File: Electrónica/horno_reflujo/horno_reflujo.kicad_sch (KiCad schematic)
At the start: 42 parts, among them J1 LevelShifter, J10 ssr1, J11 ssr2, J12 encoder, J13 Max6675_modulo2, J14 Max6675_modulo3, J15 Max6675_modulo4, J2 LevelShifter, J3 Display Oled I2C, J4 Max6675_modulo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

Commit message: Update pcb
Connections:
- net +3.3V: now also J1.3 (Pin_3); no longer J1.4 (Pin_4)
- net +5V: now also J2.4 (Pin_4), J3.2 (Pin_2); no longer J2.3 (Pin_3), J3.1 (Pin_1)
- net GND: now also J1.4 (Pin_4), J2.3 (Pin_3), J3.1 (Pin_1); no longer J1.3 (Pin_3), J2.4 (Pin_4), J3.4 (Pin_4)
- net at J2.1 (Pin_1): now also J3.3 (Pin_3); no longer J3.2 (Pin_2)
- net at J2.2 (Pin_2): now also J3.4 (Pin_4); no longer J3.3 (Pin_3)
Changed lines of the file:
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@@
 	(wire
 		(pts
+			(xy 180.34 130.81) (xy 185.42 130.81)
+		)
+		(stroke
+			(width 0)
+			(type default)
+		)
+	)
+	(wire
+		(pts
 			(xy 171.45 87.63) (xy 172.72 87.63)
 		)
@@
 	(wire
 		(pts
+			(xy 157.48 135.89) (xy 185.42 135.89)
+		)
+		(stroke
+			(width 0)
+			(type default)
+		)
+	)
+	(wire
+		(pts
 			(xy 194.31 90.17) (xy 195.58 90.17)
 		)
@@
 	(wire
 		(pts
+			(xy 157.48 119.38) (xy 157.48 135.89)
+		)
+		(stroke
+			(width 0)
+			(type default)
+		)
+	)
+	(wire
+		(pts
 			(xy 35.56 166.37) (xy 43.18 166.37)
 		)
@@
 	(wire
 		(pts
-			(xy 147.32 77.47) (xy 147.32 78.74)
+			(xy 153.67 121.92) (xy 153.67 138.43)
 		)
 		(stroke
@@
 	(wire
 		(pts
-			(xy 172.72 161.29) (xy 172.72 166.37)
+			(xy 147.32 77.47) (xy 147.32 78.74)
 		)
 		(stroke
@@
 	(wire
 		(pts
-			(xy 27.94 80.01) (xy 26.67 80.01)
+			(xy 172.72 161.29) (xy 172.72 166.37)
 		)
 		(stroke
@@
 	(wire
 		(pts
-			(xy 68.58 135.89) (xy 71.12 135.89)
+			(xy 27.94 80.01) (xy 26.67 80.01)
 		)
 		(stroke
@@
 	(wire
 		(pts
-			(xy 237.49 66.04) (xy 240.03 66.04)
+			(xy 68.58 135.89) (xy 71.12 135.89)
 		)
 		(stroke
@@
 	(wire
 		(pts
-			(xy 57.15 33.02) (xy 57.15 38.1)
+			(xy 237.49 66.04) (xy 240.03 66.04)
 		)
 		(stroke
@@
 	(wire
 		(pts
-			(xy 153.67 135.89) (xy 185.42 135.89)
+			(xy 57.15 33.02) (xy 57.15 38.1)
 		)
 		(stroke
@@
 	(wire
 		(pts
-			(xy 157.48 133.35) (xy 157.48 119.38)
+			(xy 68.58 176.53) (xy 73.66 176.53)
 		)
 		(stroke
@@
 	(wire
 		(pts
-			(xy 68.58 176.53) (xy 73.66 176.53)
+			(xy 44.45 78.74) (xy 44.45 80.01)
 		)
 		(stroke
@@
 	(wire
 		(pts
-			(xy 44.45 78.74) (xy 44.45 80.01)
+			(xy 128.27 66.04) (xy 127 66.04)
 		)
 		(stroke
@@
 	(wire
 		(pts
-			(xy 128.27 66.04) (xy 127 66.04)
+			(xy 35.56 87.63) (xy 35.56 90.17)
 		)
 		(stroke
@@
 	(wire
 		(pts
-			(xy 35.56 87.63) (xy 35.56 90.17)
+			(xy 153.67 138.43) (xy 185.42 138.43)
 		)
 		(stroke
@@
 	(wire
 		(pts
-			(xy 180.34 130.81) (xy 185.42 130.81)
+			(xy 179.07 133.35) (xy 185.42 133.35)
 		)
 		(stroke
@@
 	(wire
 		(pts
-			(xy 157.48 133.35) (xy 185.42 133.35)
-		)
-		(stroke
-			(width 0)
-			(type default)
-		)
-	)
-	(wire
-		(pts
 			(xy 166.37 95.25) (xy 172.72 95.25)
 		)
@@
 	(wire
 		(pts
-			(xy 179.07 138.43) (xy 185.42 138.43)
-		)
-		(stroke
-			(width 0)
-			(type default)
-		)
-	)
-	(wire
-		(pts
 			(xy 130.81 167.64) (xy 132.08 167.64)
 		)
@@
 	(wire
 		(pts
-			(xy 153.67 135.89) (xy 153.67 121.92)
-		)
-		(stroke
-			(width 0)
-			(type default)
-		)
-	)
-	(wire
-		(pts
 			(xy 194.31 57.15) (xy 194.31 49.53)
 		)
@@
 	(symbol
 		(lib_id "power:GND")
-		(at 144.78 127 90)
+		(at 144.78 124.46 90)
 		(unit 1)
 		(exclude_from_sim no)
@@
 		(on_board yes)
 		(dnp no)
-		(fields_autoplaced yes)
 		(property "Reference" "#PWR024"
-			(at 151.13 127 0)
+			(at 151.13 124.46 0)
 			(effects
 				(font
@@
 		)
 		(property "Value" "GND"
-			(at 148.59 126.9999 90)
+			(at 147.828 124.46 90)
 			(effects
 				(font
@@
 		)
 		(property "Footprint" ""
-			(at 144.78 127 0)
+			(at 144.78 124.46 0)
 			(effects
 				(font
@@
 		)
 		(property "Datasheet" ""
-			(at 144.78 127 0)
+			(at 144.78 124.46 0)
 			(effects
 				(font
@@
 		)
 		(property "Description" "Power symbol creates a global label with name \"GND\" , ground"
-			(at 144.78 127 0)
+			(at 144.78 124.46 0)
 			(effects
 				(font
@@
 	(symbol
 		(lib_id "power:+5V")
-		(at 180.34 130.81 90)
+		(at 179.07 133.35 90)
 		(mirror x)
 		(unit 1)
@@
 		(fields_autoplaced yes)
 		(property "Reference" "#PWR023"
-			(at 184.15 130.81 0)
+			(at 182.88 133.35 0)
 			(effects
 				(font
@@
 		)
 		(property "Value" "+5V"
-			(at 176.53 130.8099 90)
+			(at 175.26 133.3499 90)
 			(effects
 				(font
@@
 		)
 		(property "Footprint" ""
-			(at 180.34 130.81 0)
+			(at 179.07 133.35 0)
 			(effects
 				(font
@@
 		)
 		(property "Datasheet" ""
-			(at 180.34 130.81 0)
+			(at 179.07 133.35 0)
 			(effects
 				(font
@@
 		)
 		(property "Description" "Power symbol creates a global label with name \"+5V\""
-			(at 180.34 130.81 0)
+			(at 179.07 133.35 0)
 			(effects
 				(font
@@
 	(symbol
 		(lib_id "PCM_4ms_Power-symbol:+3.3V")
-		(at 123.19 124.46 90)
+		(at 123.19 127 90)
 		(unit 1)
 		(exclude_from_sim no)
@@
 		(on_board yes)
 		(dnp no)
-		(fields_autoplaced yes)
 		(property "Reference" "#PWR051"
-			(at 127 124.46 0)
+			(at 127 127 0)
 			(effects
 				(font
@@
 		)
 		(property "Value" "+3.3V"
-			(at 119.38 124.4599 90)
+			(at 119.38 127 90)
 			(effects
 				(font
@@
 		)
 		(property "Footprint" ""
-			(at 123.19 124.46 0)
+			(at 123.19 127 0)
 			(effects
 				(font
@@
 		)
 		(property "Datasheet" ""
-			(at 123.19 124.46 0)
+			(at 123.19 127 0)
 			(effects
 				(font
@@
 		)
 		(property "Description" ""
-			(at 123.19 124.46 0)
+			(at 123.19 127 0)
 			(effects
 				(font
@@
 	(symbol
 		(lib_id "power:GND")
-		(at 123.19 127 270)
+		(at 123.19 124.46 270)
 		(unit 1)
 		(exclude_from_sim no)
@@
 		(fields_autoplaced yes)
 		(property "Reference" "#PWR020"
-			(at 116.84 127 0)
+			(at 116.84 124.46 0)
 			(effects
 				(font
@@
 		)
 		(property "Value" "GND"
-			(at 119.38 126.9999 90)
+			(at 119.38 124.4599 90)
 			(effects
 				(font
@@
 		)
 		(property "Footprint" ""
-			(at 123.19 127 0)
+			(at 123.19 124.46 0)
 			(effects
 				(font
@@
 		)
 		(property "Datasheet" ""
-			(at 123.19 127 0)
+			(at 123.19 124.46 0)
 			(effects
 				(font
@@
 		)
 		(property "Description" "Power symbol creates a global label with name \"GND\" , ground"
-			(at 123.19 127 0)
+			(at 123.19 124.46 0)
 			(effects
 				(font
@@
 	(symbol
 		(lib_id "power:GND")
-		(at 179.07 138.43 270)
+		(at 180.34 130.81 270)
 		(mirror x)
 		(unit 1)
@@
 		(fields_autoplaced yes)
 		(property "Reference" "#PWR022"
-			(at 172.72 138.43 0)
+			(at 173.99 130.81 0)
 			(effects
 				(font
@@
 		)
 		(property "Value" "GND"
-			(at 175.26 138.4299 90)
+			(at 176.53 130.8099 90)
 			(effects
 				(font
@@
 		)
 		(property "Footprint" ""
-			(at 179.07 138.43 0)
+			(at 180.34 130.81 0)
 			(effects
 				(font
@@
 		)
 		(property "Datasheet" ""
-			(at 179.07 138.43 0)
+			(at 180.34 130.81 0)
 			(effects
 				(font
@@
 		)
 		(property "Description" "Power symbol creates a global label with name \"GND\" , ground"
-			(at 179.07 138.43 0)
+			(at 180.34 130.81 0)
 			(effects
 				(font
@@
 	(symbol
 		(lib_id "power:+5V")
-		(at 144.78 124.46 270)
+		(at 144.78 127 270)
 		(unit 1)
 		(exclude_from_sim no)
@@
 		(fields_autoplaced yes)
 		(property "Reference" "#PWR06"
-			(at 140.97 124.46 0)
+			(at 140.97 127 0)
 			(effects
 				(font
@@
 		)
 		(property "Value" "+5V"
-			(at 148.59 124.4599 90)
+			(at 148.59 126.9999 90)
 			(effects
 				(font
@@
 		)
 		(property "Footprint" ""
-			(at 144.78 124.46 0)
+			(at 144.78 127 0)
 			(effects
 				(font
@@
 		)
 		(property "Datasheet" ""
-			(at 144.78 124.46 0)
+			(at 144.78 127 0)
 			(effects
 				(font
@@
 		)
 		(property "Description" "Power symbol creates a global label with name \"+5V\""
-			(at 144.78 124.46 0)
+			(at 144.78 127 0)
 			(effects
 				(font

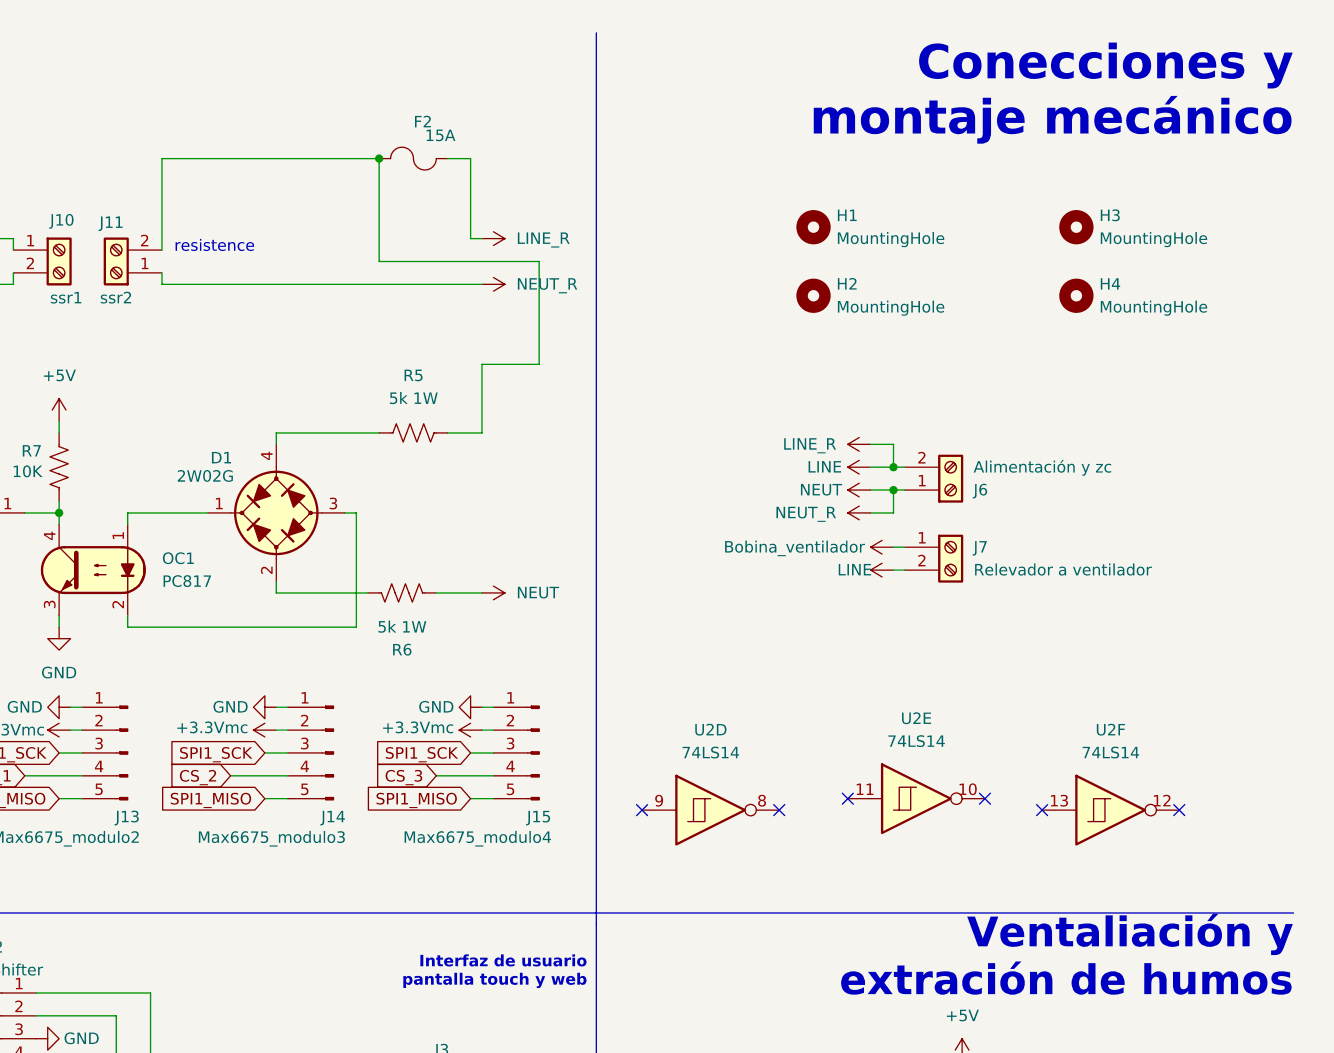
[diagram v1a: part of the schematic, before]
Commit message: 74ls04 inputs are now grounded
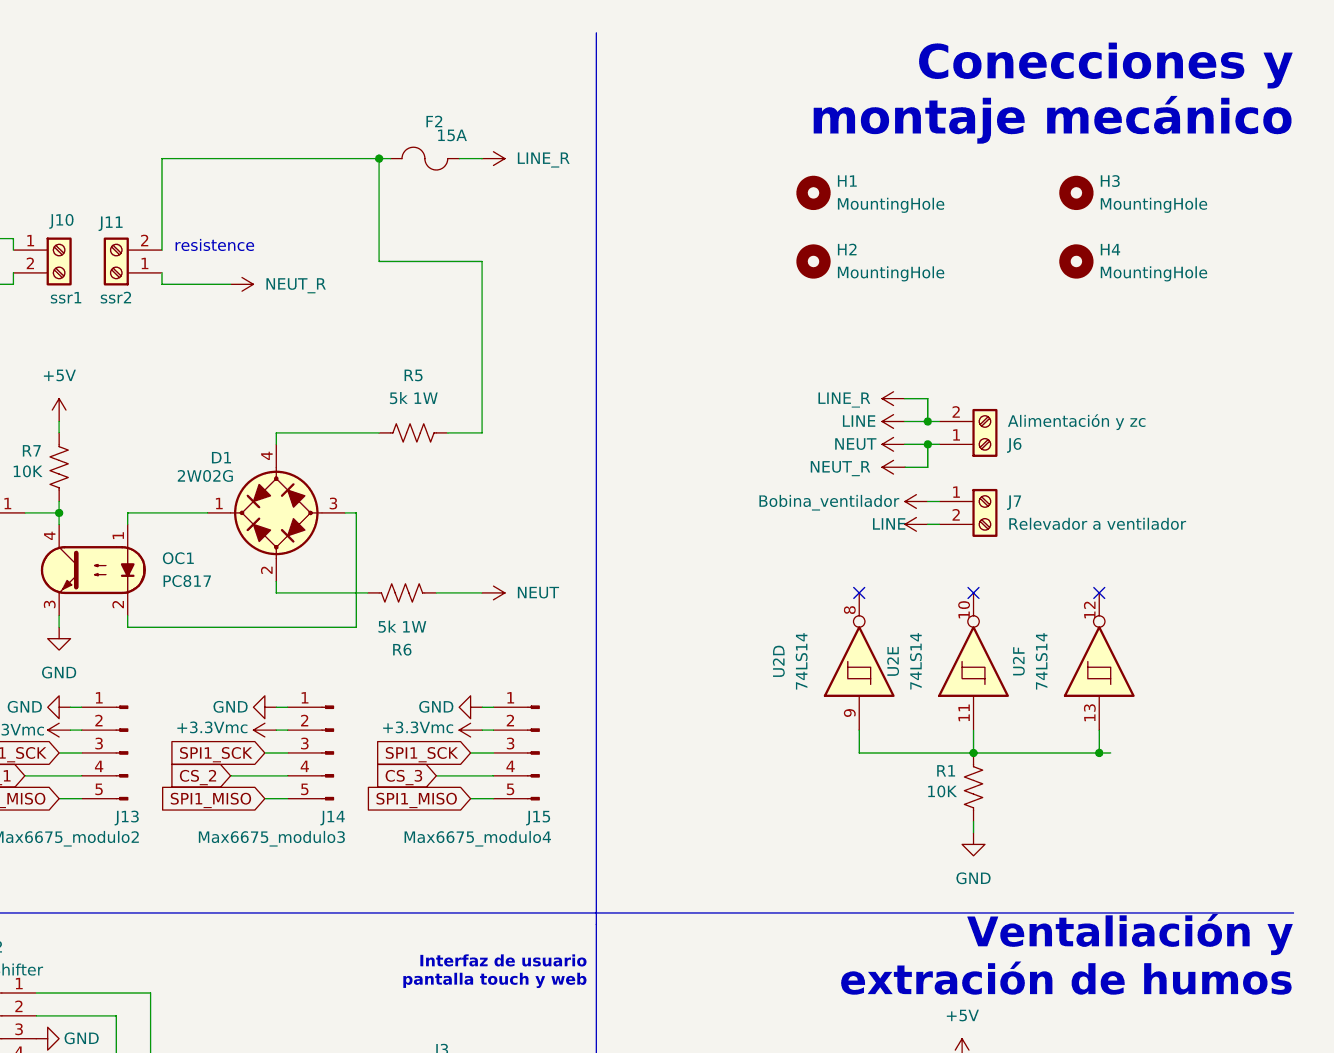
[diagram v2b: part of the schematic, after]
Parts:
- added R1: 10K, Resistor_THT:R_Axial_DIN0207_L6.3mm_D2.5mm_P2.54mm_Vertical, symbol Device:R_US
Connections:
- net GND: now also R1.1
- net at U2.9: now also U2.11, U2.13, R1.2
- no-connect marks 10 -> 7
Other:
- moved on the sheet: F2, H1, H2, H3, H4, J6, J7, U2D, U2E, U2F

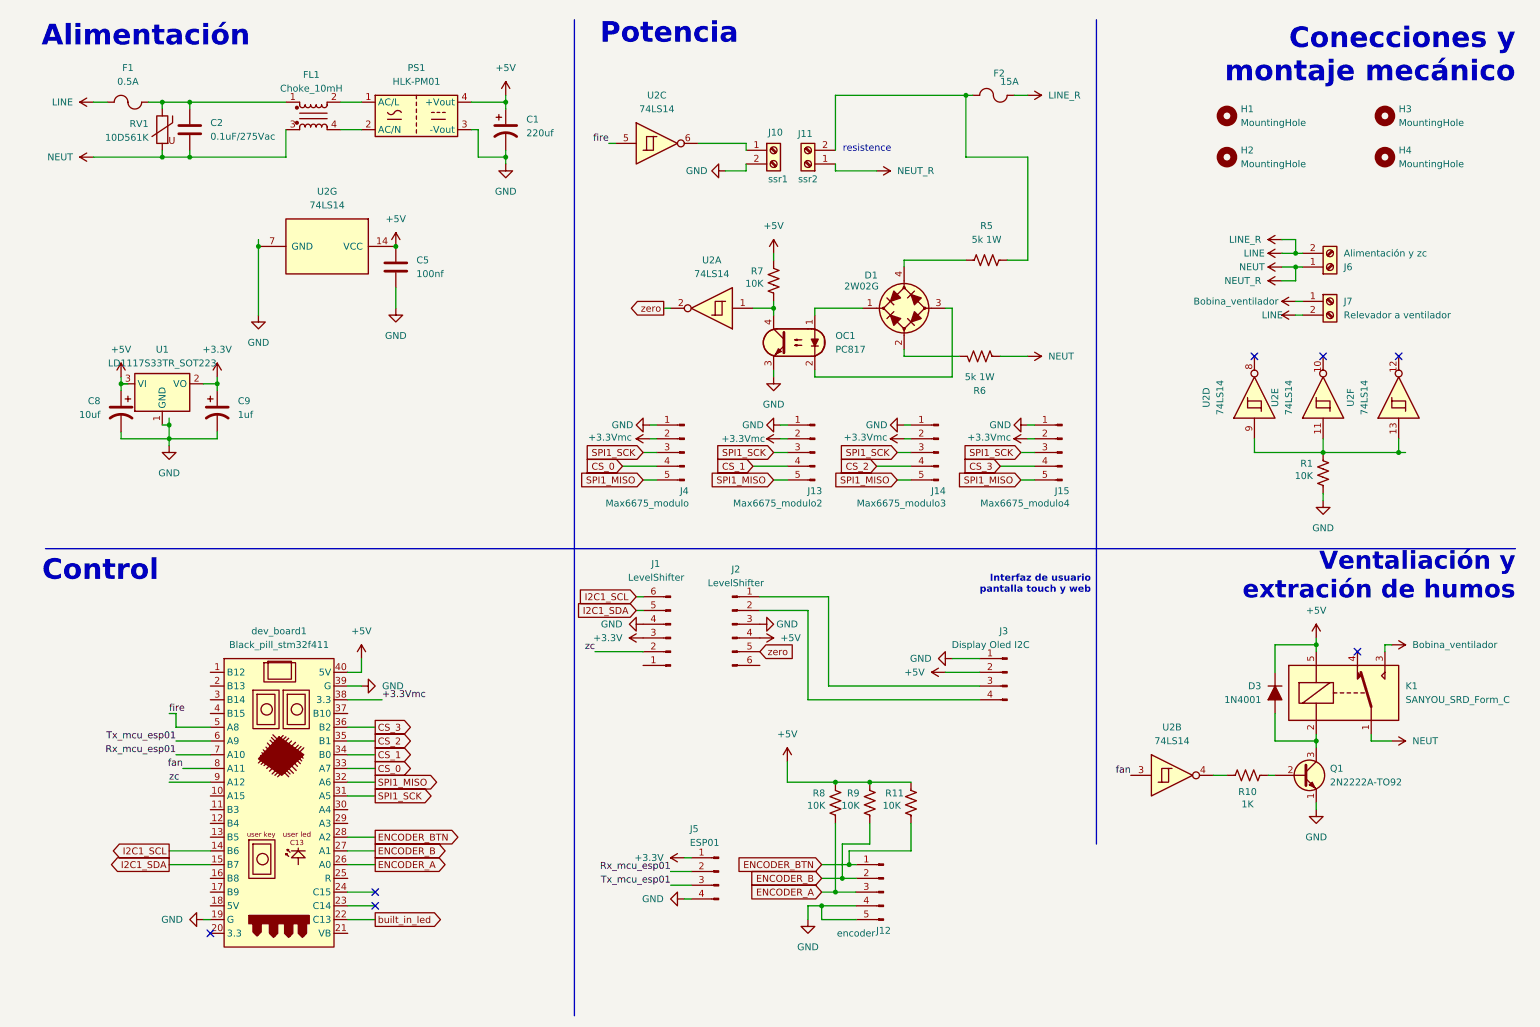
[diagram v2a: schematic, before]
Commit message: 74ls04 inputs now have pull-up/down resistors
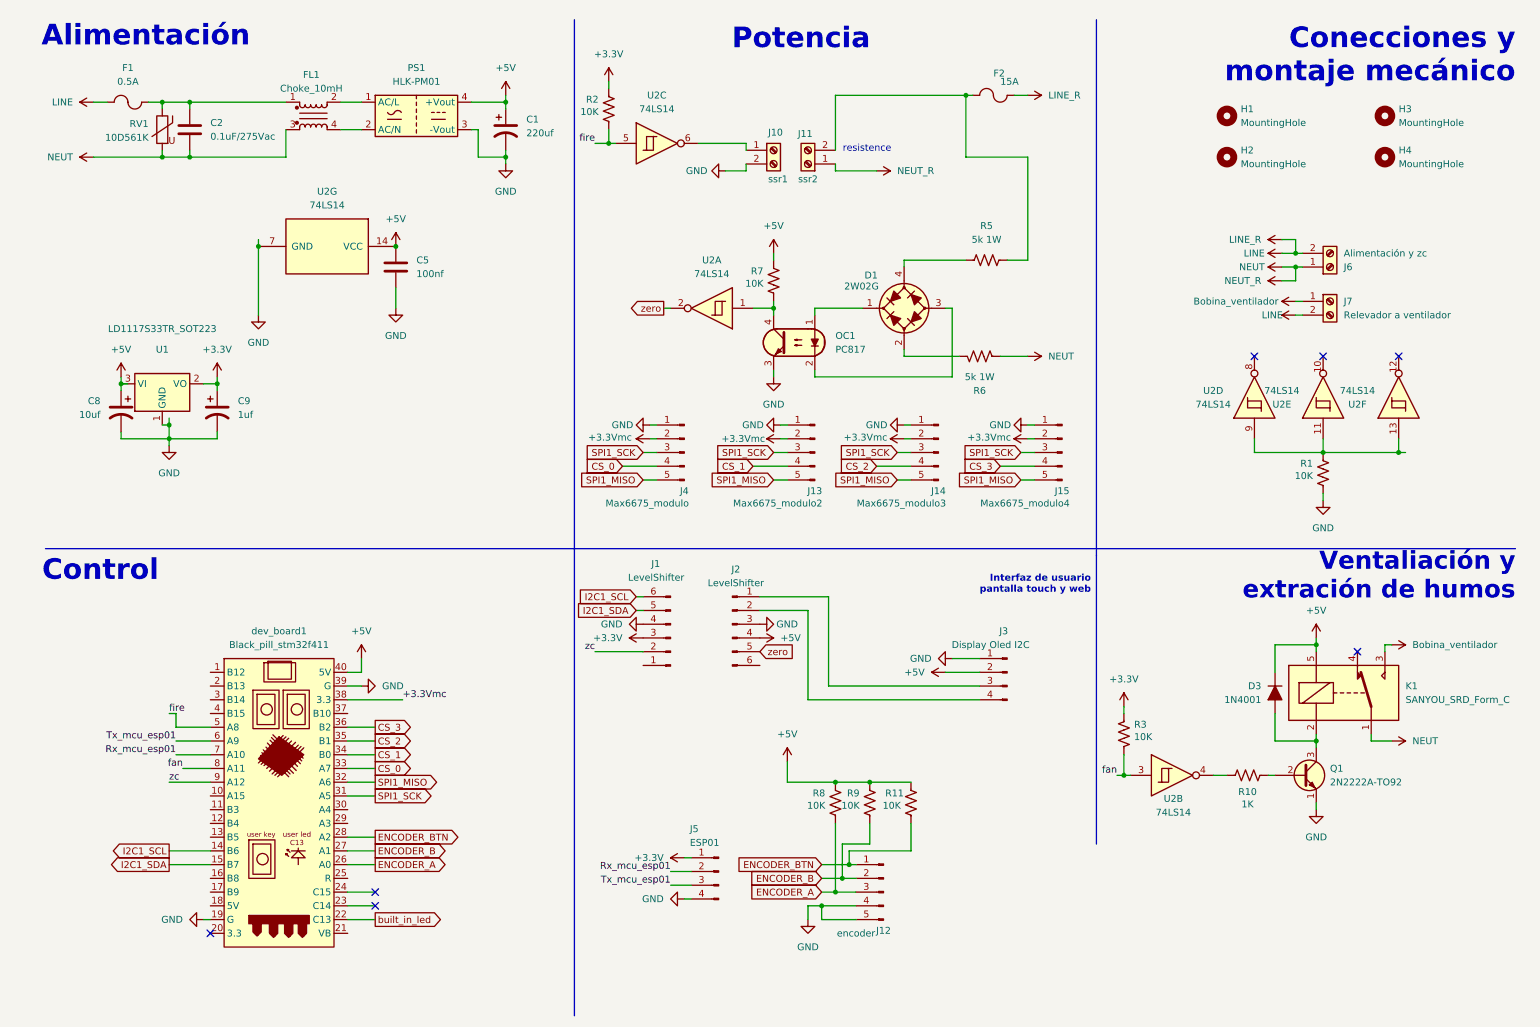
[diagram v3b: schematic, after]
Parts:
- added R2, R3: 10K, Resistor_THT:R_Axial_DIN0207_L6.3mm_D2.5mm_P2.54mm_Vertical, symbol Device:R_US
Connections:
- net +3.3V: now also R2.2, R3.2
- net fan: now also R3.1
- net fire: now also R2.1
